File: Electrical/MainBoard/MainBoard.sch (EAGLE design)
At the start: 121 parts, among them IC1 MEGA16-P, IC2 MCP4922-E/SL, IC3 MCP4921-E/SN, IC4 TL074D, IC5 TL074D, IC6 FT232RL, Q1 BC140-10, Q2 BC160, Q3 BC140-10, Q4 BC160, Q5 BD239, Q6 BD240, Q7 BC557, Q8 16MHz, X1 FH12-45S-0.5SH, X2 22-23-2021, X3 PN61729-S

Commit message: Board resized
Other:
- note added: "PowerSupply SigGen v1.1"
- note removed: "PowerSupply SigGen v1.0"

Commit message: Resistors add to MainBoard to convert 5V to 3.3V for LCD signals
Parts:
- added R39, R40, R41, R42: 1k, OwnDevices:R-EU_R0805
- added R43, R44, R45, R46: 2k4, OwnDevices:R-EU_R0805
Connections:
- net DDS_CS renamed !DDS_CS
- net DDS_LDAC renamed !DDS_LDAC
- net PS_CS renamed !PS_CS
- removed net LCD_CS: IC1.(T1)PB1, X1-3.1
- new net !LCD_CS: IC1.(T1)PB1, R39.2
- new net !LCD_CS_3V3: R39.1, R43.1, X1-3.1
- new net LCD_A0_3V3: R40.1, R44.1, X1-7.1
- new net MOSI_3V3: R42.1, R46.1, X1-11.1
- new net SCK_3V3: R41.1, R45.1, X1-9.1
- net GND: now also R43.2, R44.2, R45.2, R46.2
- net LCD_A0: now also R40.2; no longer X1-7.1
- net MOSI: now also R42.2; no longer X1-11.1
- net SCK: now also R41.2; no longer X1-9.1
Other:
- note added: "PowerSupply SigGen v1.2"
- note removed: "PowerSupply SigGen v1.1"

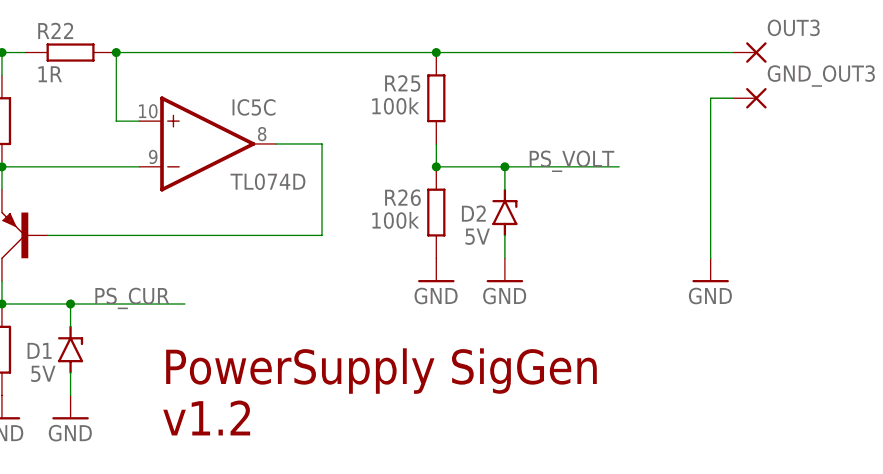
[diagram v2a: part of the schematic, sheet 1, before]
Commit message: Updated to new project name (PS_Fgen_HW), removed Z-Diode and ATX_PWR_ON signal from MainBoard
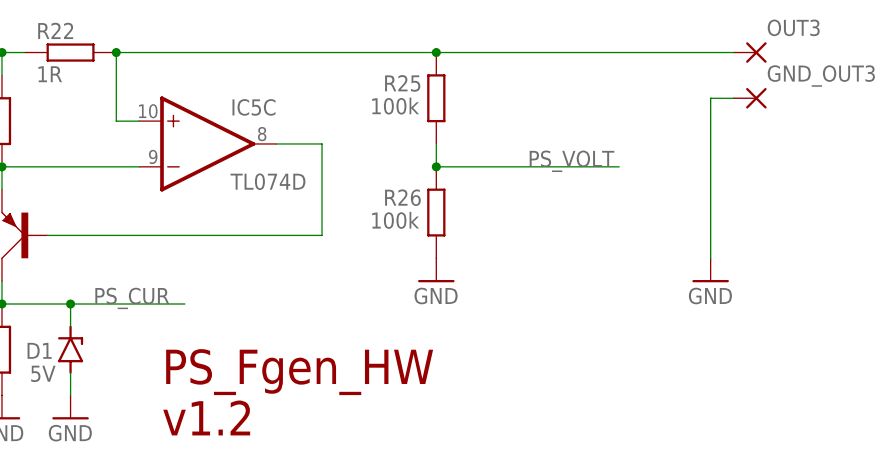
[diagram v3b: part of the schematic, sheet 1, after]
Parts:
- removed ATX_PWRON: (no value), OwnDevices:2,54/1,0
- removed D2: 5V, diode:ZENER-DIODESOD80C
- IC1: value MEGA16-P -> MEGA1284-P
- R43, R44, R45, R46: value 2k4 -> 2k
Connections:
- removed net ATX_PWR_ON: ATX_PWRON.P, IC1.(OC1A)PD5
- net GND: no longer D2.A
- net PS_VOLT: no longer D2.C
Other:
- note added: "PS_Fgen_HW v1.2"
- note removed: "PowerSupply SigGen v1.2"
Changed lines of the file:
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@@
 <?xml version="1.0" encoding="utf-8"?>
 <!DOCTYPE eagle SYSTEM "eagle.dtd">
-<eagle version="9.5.2">
+<eagle version="9.6.2">
 <drawing>
 <settings>
@@
 </classes>
 <parts>
-<part name="IC1" library="atmel" library_urn="urn:adsk.eagle:library:105" deviceset="MEGA16-P" device="" package3d_urn="urn:adsk.eagle:package:4314/1" override_package3d_urn="urn:adsk.eagle:package:22513599/2" override_package_urn="urn:adsk.eagle:footprint:4151/1"/>
+<part name="IC1" library="atmel" library_urn="urn:adsk.eagle:library:105" deviceset="MEGA16-P" device="" package3d_urn="urn:adsk.eagle:package:4314/1" override_package3d_urn="urn:adsk.eagle:package:22513599/2" override_package_urn="urn:adsk.eagle:footprint:4151/1" value="MEGA1284-P"/>
 <part name="IC2" library="nh-ic" deviceset="MCP4922" device="-E/SL" override_package3d_urn="urn:adsk.eagle:package:22514112/2" override_package_urn="urn:adsk.eagle:footprint:22514113/1"/>
 <part name="IC3" library="nh-ic" deviceset="MCP4921" device="-E/SN" override_package3d_urn="urn:adsk.eagle:package:22514205/2" override_package_urn="urn:adsk.eagle:footprint:22514206/1"/>
@@
 <part name="GND9" library="supply1" library_urn="urn:adsk.eagle:library:371" deviceset="GND" device=""/>
 <part name="D1" library="diode" library_urn="urn:adsk.eagle:library:210" deviceset="ZENER-DIODE" device="SOD80C" package3d_urn="urn:adsk.eagle:package:43405/2" value="5V"/>
-<part name="D2" library="diode" library_urn="urn:adsk.eagle:library:210" deviceset="ZENER-DIODE" device="SOD80C" package3d_urn="urn:adsk.eagle:package:43405/2" value="5V"/>
 <part name="GND10" library="supply1" library_urn="urn:adsk.eagle:library:371" deviceset="GND" device=""/>
-<part name="GND11" library="supply1" library_urn="urn:adsk.eagle:library:371" deviceset="GND" device=""/>
 <part name="FRAME1" library="frames" library_urn="urn:adsk.eagle:library:229" deviceset="A4L-LOC" device=""/>
 <part name="FRAME2" library="frames" library_urn="urn:adsk.eagle:library:229" deviceset="A4L-LOC" device=""/>
@@
 <part name="GND_3" library="OwnDevices" library_urn="urn:adsk.eagle:library:19498084" deviceset="2,54/1,0" device="" package3d_urn="urn:adsk.eagle:package:30828/1"/>
 <part name="GND_4" library="OwnDevices" library_urn="urn:adsk.eagle:library:19498084" deviceset="2,54/1,0" device="" package3d_urn="urn:adsk.eagle:package:30828/1"/>
-<part name="ATX_PWRON" library="OwnDevices" library_urn="urn:adsk.eagle:library:19498084" deviceset="2,54/1,0" device="" package3d_urn="urn:adsk.eagle:package:30828/1"/>
 <part name="LED1" library="led" library_urn="urn:adsk.eagle:library:259" deviceset="TOPLED-2-" device="-" package3d_urn="urn:adsk.eagle:package:15835/1" override_package3d_urn="urn:adsk.eagle:package:22514101/2" override_package_urn="urn:adsk.eagle:footprint:15690/1"/>
 <part name="P+22" library="supply1" library_urn="urn:adsk.eagle:library:371" deviceset="VCC" device=""/>
@@
 <part name="R41" library="OwnDevices" library_urn="urn:adsk.eagle:library:19498084" deviceset="R-EU_" device="R0805" package3d_urn="urn:adsk.eagle:package:23553/2" value="1k"/>
 <part name="R42" library="OwnDevices" library_urn="urn:adsk.eagle:library:19498084" deviceset="R-EU_" device="R0805" package3d_urn="urn:adsk.eagle:package:23553/2" value="1k"/>
-<part name="R43" library="OwnDevices" library_urn="urn:adsk.eagle:library:19498084" deviceset="R-EU_" device="R0805" package3d_urn="urn:adsk.eagle:package:23553/2" value="2k4"/>
-<part name="R44" library="OwnDevices" library_urn="urn:adsk.eagle:library:19498084" deviceset="R-EU_" device="R0805" package3d_urn="urn:adsk.eagle:package:23553/2" value="2k4"/>
-<part name="R45" library="OwnDevices" library_urn="urn:adsk.eagle:library:19498084" deviceset="R-EU_" device="R0805" package3d_urn="urn:adsk.eagle:package:23553/2" value="2k4"/>
-<part name="R46" library="OwnDevices" library_urn="urn:adsk.eagle:library:19498084" deviceset="R-EU_" device="R0805" package3d_urn="urn:adsk.eagle:package:23553/2" value="2k4"/>
+<part name="R43" library="OwnDevices" library_urn="urn:adsk.eagle:library:19498084" deviceset="R-EU_" device="R0805" package3d_urn="urn:adsk.eagle:package:23553/2" value="2k"/>
+<part name="R44" library="OwnDevices" library_urn="urn:adsk.eagle:library:19498084" deviceset="R-EU_" device="R0805" package3d_urn="urn:adsk.eagle:package:23553/2" value="2k"/>
+<part name="R45" library="OwnDevices" library_urn="urn:adsk.eagle:library:19498084" deviceset="R-EU_" device="R0805" package3d_urn="urn:adsk.eagle:package:23553/2" value="2k"/>
+<part name="R46" library="OwnDevices" library_urn="urn:adsk.eagle:library:19498084" deviceset="R-EU_" device="R0805" package3d_urn="urn:adsk.eagle:package:23553/2" value="2k"/>
 <part name="GND46" library="supply1" library_urn="urn:adsk.eagle:library:371" deviceset="GND" device=""/>
 <part name="GND47" library="supply1" library_urn="urn:adsk.eagle:library:371" deviceset="GND" device=""/>
@@
 <sheet>
 <plain>
-<text x="162.56" y="22.86" size="3.81" layer="94" align="top-left">PowerSupply SigGen
+<text x="162.56" y="22.86" size="3.81" layer="94" align="top-left">PS_Fgen_HW
 v1.2</text>
 <text x="50.8" y="134.62" size="3.81" layer="97">DDS1 / DDS2</text>
@@
 <attribute name="VALUE" x="150.749" y="21.082" size="1.778" layer="96" rot="R180"/>
 </instance>
-<instance part="D2" gate="G$1" x="200.66" y="38.1" smashed="yes" rot="R90">
-<attribute name="NAME" x="198.755" y="38.862" size="1.778" layer="95" rot="R180"/>
-<attribute name="VALUE" x="199.009" y="36.322" size="1.778" layer="96" rot="R180"/>
-</instance>
 <instance part="GND10" gate="1" x="152.4" y="15.24" smashed="yes">
 <attribute name="VALUE" x="149.86" y="12.7" size="1.778" layer="96"/>
-</instance>
-<instance part="GND11" gate="1" x="200.66" y="30.48" smashed="yes">
-<attribute name="VALUE" x="198.12" y="27.94" size="1.778" layer="96"/>
 </instance>
 <instance part="FRAME1" gate="G$1" x="0" y="0" smashed="yes">
@@
 <pinref part="D1" gate="G$1" pin="A"/>
 <wire x1="152.4" y1="17.78" x2="152.4" y2="20.32" width="0.1524" layer="91"/>
-</segment>
-<segment>
-<pinref part="GND11" gate="1" pin="GND"/>
-<pinref part="D2" gate="G$1" pin="A"/>
-<wire x1="200.66" y1="33.02" x2="200.66" y2="35.56" width="0.1524" layer="91"/>
 </segment>
 <segment>
@@
 <pinref part="R26" gate="G$1" pin="2"/>
 <wire x1="193.04" y1="45.72" x2="193.04" y2="43.18" width="0.1524" layer="91"/>
-<pinref part="D2" gate="G$1" pin="C"/>
-<wire x1="200.66" y1="40.64" x2="200.66" y2="43.18" width="0.1524" layer="91"/>
-<wire x1="200.66" y1="43.18" x2="193.04" y2="43.18" width="0.1524" layer="91"/>
 <junction x="193.04" y="43.18"/>
-<wire x1="213.36" y1="43.18" x2="200.66" y2="43.18" width="0.1524" layer="91"/>
-<junction x="200.66" y="43.18"/>
+<wire x1="213.36" y1="43.18" x2="193.04" y2="43.18" width="0.1524" layer="91"/>
 <label x="203.2" y="43.18" size="1.778" layer="95"/>
 </segment>
@@
 <plain>
 <text x="223.52" y="167.64" size="1.778" layer="91">(RST)</text>
-<text x="162.56" y="22.86" size="3.81" layer="94" align="top-left">PowerSupply SigGen
+<text x="162.56" y="22.86" size="3.81" layer="94" align="top-left">PS_Fgen_HW
 v1.2</text>
 <text x="154.94" y="172.72" size="3.81" layer="97" align="top-left">Display</text>
@@
 <attribute name="NAME" x="57.023" y="93.2942" size="1.778" layer="95"/>
 <attribute name="VALUE" x="59.563" y="88.138" size="1.778" layer="96" rot="MR0"/>
-</instance>
-<instance part="ATX_PWRON" gate="P" x="15.24" y="78.74" smashed="yes">
-<attribute name="NAME" x="14.097" y="80.5942" size="1.778" layer="95"/>
-<attribute name="VALUE" x="14.097" y="75.438" size="1.778" layer="96"/>
 </instance>
 <instance part="X2" gate="-1" x="233.68" y="43.18" smashed="yes">
@@
 </segment>
 </net>
-<net name="ATX_PWR_ON" class="0">
-<segment>
-<pinref part="ATX_PWRON" gate="P" pin="P"/>
-<wire x1="17.78" y1="78.74" x2="60.96" y2="78.74" width="0.1524" layer="91"/>
-<label x="35.56" y="78.74" size="1.778" layer="95"/>
-</segment>
-</net>
 <net name="BL_A" class="0">
 <segment>
@@
 <text x="231.14" y="68.58" size="1.778" layer="91" rot="R90">TX / green</text>
 <text x="246.38" y="68.58" size="1.778" layer="91" rot="R90">RX / red</text>
-<text x="162.56" y="22.86" size="3.81" layer="94" align="top-left">PowerSupply SigGen
+<text x="162.56" y="22.86" size="3.81" layer="94" align="top-left">PS_Fgen_HW
 v1.2</text>
 <text x="22.86" y="162.56" size="3.81" layer="97" align="top-left">Microcontroller</text>
@@
 </segment>
 </net>
-<net name="ATX_PWR_ON" class="0">
-<segment>
-<pinref part="IC1" gate="G$1" pin="(OC1A)PD5"/>
-<wire x1="88.9" y1="71.12" x2="106.68" y2="71.12" width="0.1524" layer="91"/>
-<label x="93.98" y="71.12" size="1.778" layer="95"/>
-</segment>
-</net>

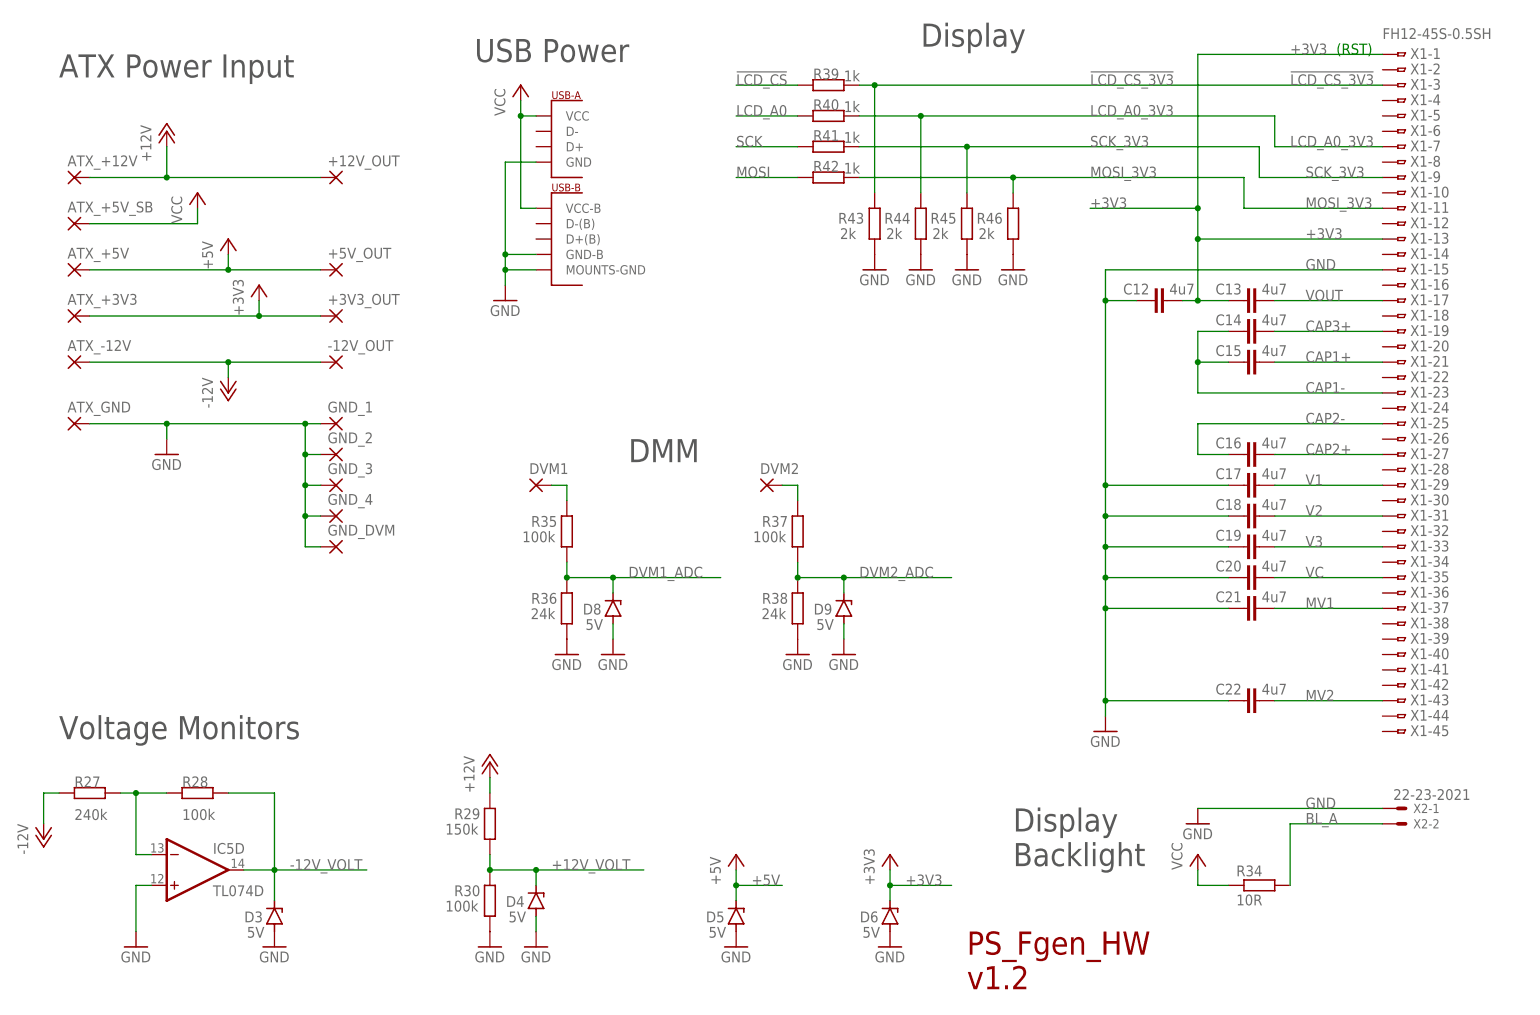
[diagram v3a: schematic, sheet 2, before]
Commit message: MainBoard: Removed ATX_5V_SB input (combined VCC and +5V nets)
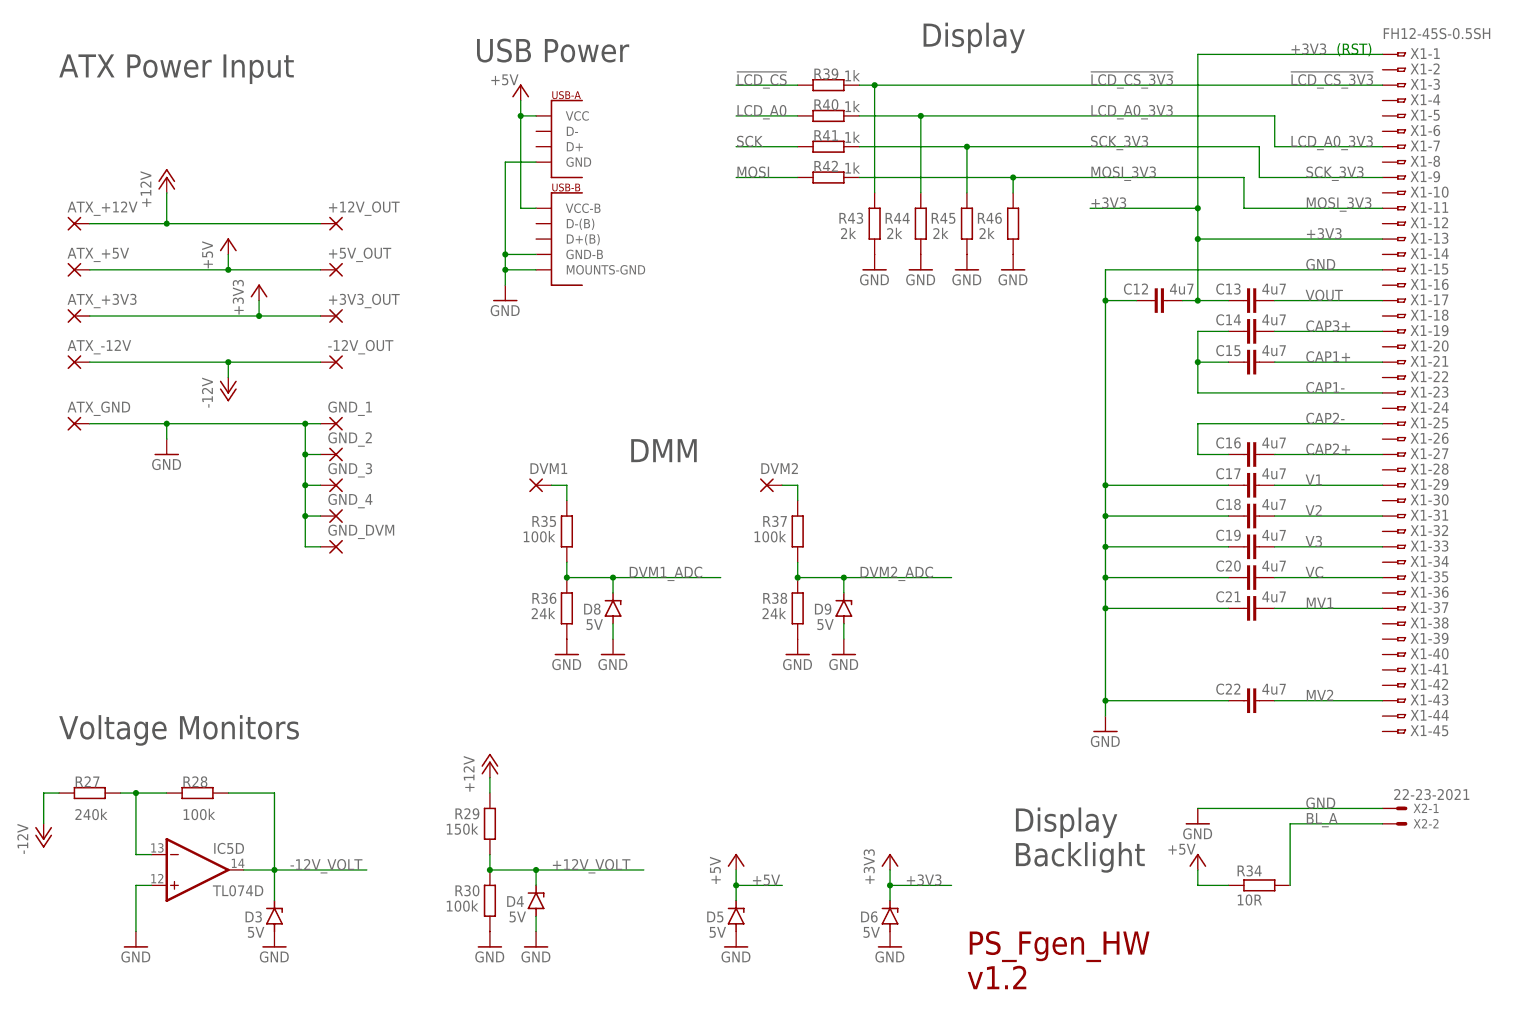
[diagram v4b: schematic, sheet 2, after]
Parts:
- removed ATX_+5V_SB: (no value), OwnDevices:2,54/1,0
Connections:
- removed net VCC: ATX_+5V_SB.P, C10.1, C8.2, C9.+, D7.C, IC1.AREF, IC1.AVCC, IC1.VCC, IC6.VCC, IC6.VCCIO, R31.2, R32.2, R33.2, R34.1, SV1.2, U$2.VCC, U$2.VCC-B, X3.1
- net +5V: now also C10.1, C8.2, C9.+, D7.C, IC1.AREF, IC1.AVCC, IC1.VCC, IC6.VCC, IC6.VCCIO, R31.2, R32.2, R33.2, R34.1, SV1.2, U$2.VCC, U$2.VCC-B, X3.1
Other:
- moved on the sheet: +12V_OUT, ATX_+12V
